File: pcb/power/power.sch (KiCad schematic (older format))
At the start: 48 parts, among them CON1 BARREL_JACK, P1 CONN_01X04, P2 CONN_01X04, P3 CONN_01X04, P4 USB_B, P5 CONN_01X03, P6 CONN_01X03, U1 TS30013, U2 LM324QT, U3 LM2840

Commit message: Added some more footprints. Maybe have to change some grounding stuff.
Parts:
- removed D4: VS-10MQ060NPbF, symbol D_Schottky
- removed P1: CONN_01X04, symbol CONN_01X04
- removed P4: USB_B, symbol USB_B
- removed P6: CONN_01X03, symbol CONN_01X03
- removed U1: TS30013, symbol TS30013
- added D?: VS-10MQ060NPbF, Diodes_SMD:SMA_Handsoldering, symbol D_Schottky
- added P?: USB_A, Connect:USB_A, symbol USB_A
- added P?: CONN_01X04, Pin_Headers:Pin_Header_Straight_1x04, symbol CONN_01X04
- added P?: CONN_01X03, Pin_Headers:Pin_Header_Straight_1x03, symbol CONN_01X03
- added U?: TS30012, Additional:QFN-16-1EP_3x3mm_Pitch0.5mm, symbol TS30012
- C1, C11, C2, C3, C4, C6, C8: footprint (none) -> Capacitors_SMD:C_0603_HandSoldering
- D2: footprint (none) -> Diodes_SMD:SMA_Handsoldering
- D3, D5: footprint (none) -> LEDs:LED_0603
- L1: footprint (none) -> Additional:Taiyo_Yuden_NRS8030_IND
- L2: footprint (none) -> Additional:Bourns_SRN3015
- P2: footprint (none) -> Pin_Headers:Pin_Header_Straight_1x04; Digikey (none) -> S7002-ND
- P5: footprint (none) -> Pin_Headers:Pin_Header_Straight_1x03; Digikey (none) -> S7036-ND
- R10, R11, R12: footprint (none) -> Resistors_SMD:R_0603_HandSoldering
- R20: Digikey (none) -> 311-560GRCT-ND
- R6: footprint (none) -> Capacitors_SMD:C_0603_HandSoldering; Digikey (none) -> 311-1.5KGRCT-ND
- U3: footprint (none) -> TO_SOT_Packages_SMD:SOT-23-6
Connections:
- net labels added: GNDPWR
- wire segments 142 -> 140
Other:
- note added: "5V for Mobile Phone\n-----------------------\nVout,max=5 V\nAout,max = 2A"
- note added: "Bucket Converter\n---------------------------\nVout=0.765 V (1 + (27k/ 10.15k))=2.8 V\n27k/10.15k= 2.66"
- note removed: "Bucket Converter\n---------------------------\nVout=0.765 V (1 + (27k/ 10.15k))=2.8 V\n27k/10.15= 2.66"
- moved on the sheet: R6

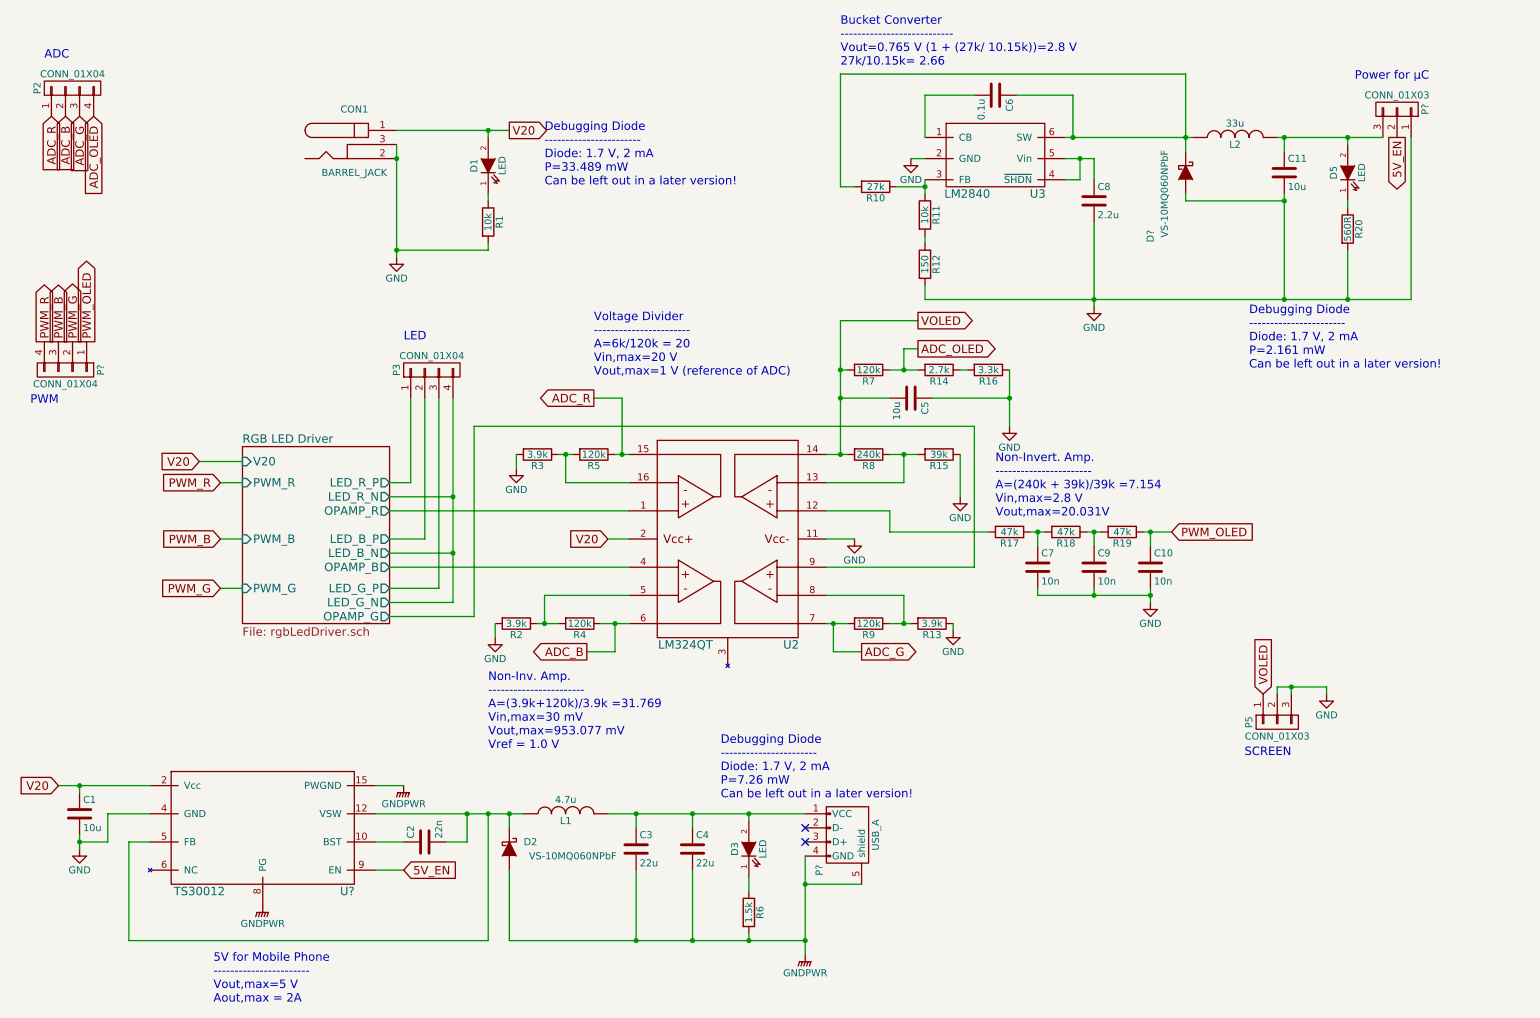
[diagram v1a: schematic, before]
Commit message: All footprints assigned. No DRC errors anymore.
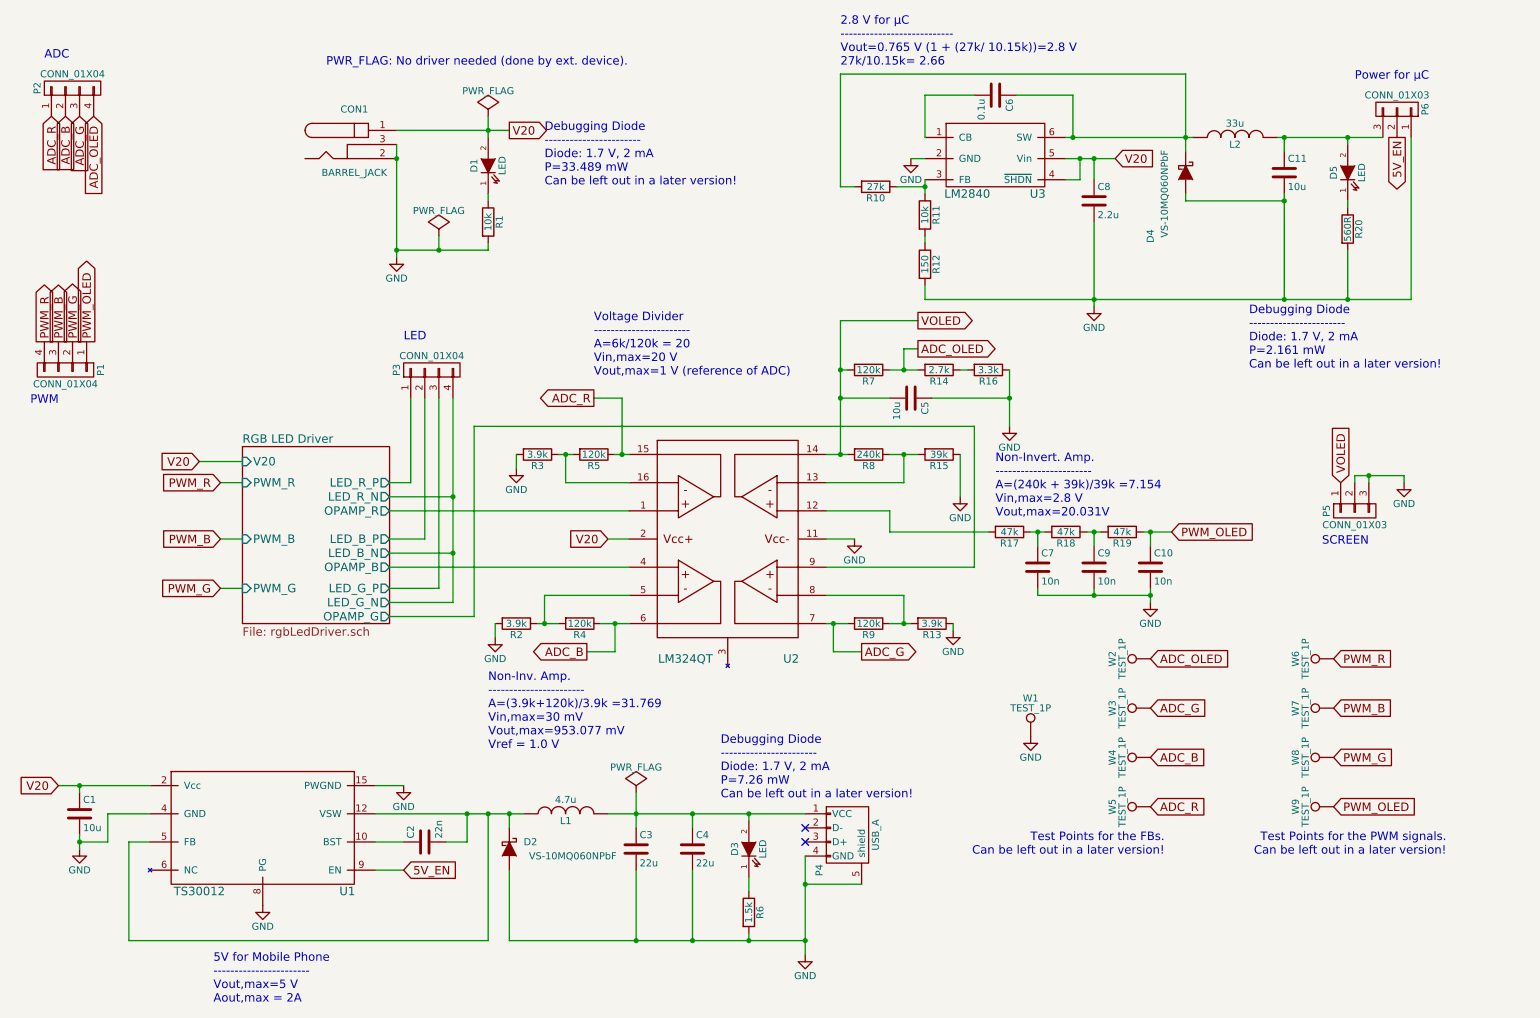
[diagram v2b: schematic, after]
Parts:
- added W1: TEST_1P, Measurement_Points:Measurement_Point_Round-SMD-Pad_Big, symbol TEST_1P
- added W2, W3, W4, W5, W6, W7, W8, W9: TEST_1P, Additional:TP_PROBE, symbol TEST_1P
- C10, C5, C7, C9: footprint (none) -> Capacitors_SMD:C_0603_HandSoldering
- D1: footprint (none) -> LEDs:LED_0603
- P3: footprint (none) -> Connect:PINHEAD1-3; Digikey ED2611-ND -> ED10563-ND
- R1: footprint (none) -> Resistors_SMD:R_0603_HandSoldering; Digikey (none) -> 311-10.0KHRCT-ND
- R13, R14, R15, R16, R17, R18, R19, R2, R20, R3, R4, R5, R7, R8, R9: footprint (none) -> Resistors_SMD:R_0603_HandSoldering
- U2: footprint (none) -> Additional:QFN-16-1EP_3x3mm_Pitch0.5mm
- gave numbers to parts that had none: 5
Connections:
- net GNDPWR is gone; now on net GND: C3.2, C4.2, D2.2 (A), P4.4 (GND), P4.5 (shield), R6.2, U1.14 (PWGND), U1.15 (PWGND), U1.8 (PG)
- net ADC_B: now also W4.1
- net ADC_G: now also W3.1
- net ADC_OLED: now also W2.1
- net ADC_R: now also W5.1
- net GND: now also W1.1
- net PWM_B: now also W7.1
- net PWM_G: now also W8.1
- net PWM_OLED: now also W9.1
- net PWM_R: now also W6.1
- net Vcc: now also C8.1, U3.4 (~SHDN), U3.5 (Vin)
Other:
- note added: "2.8 V for µC\n---------------------------\nVout=0.765 V (1 + (27k/ 10.15k))=2.8 V\n27k/10.15k= 2.66"
- note added: "PWR_FLAG: No driver needed (done by ext. device)."
- note added: "Test Points for the FBs.\nCan be left out in a later version!"
- note added: "Test Points for the PWM signals.\nCan be left out in a later version!"
- note removed: "Bucket Converter\n---------------------------\nVout=0.765 V (1 + (27k/ 10.15k))=2.8 V\n27k/10.15k= 2.66"
- moved on the sheet: P5

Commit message: Finished the schematics.
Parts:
- removed C1, C11, C5: 10u, Capacitors_SMD:C_0603_HandSoldering, symbol C
- removed C10, C7, C9: 10n, Capacitors_SMD:C_0603_HandSoldering, symbol C
- removed C2: 22n, Capacitors_SMD:C_0603_HandSoldering, symbol C
- removed C3, C4: 22u, Capacitors_SMD:C_0603_HandSoldering, symbol C
- removed C6: 0.1u, Capacitors_SMD:C_0603_HandSoldering, symbol C
- removed C8: 2.2u, Capacitors_SMD:C_0603_HandSoldering, symbol C
- removed D2, D4: VS-10MQ060NPbF, Diodes_SMD:SMA_Handsoldering, symbol D_Schottky
- removed D3, D5: LED, LEDs:LED_0603, symbol LED
- removed L1: 4.7u, Additional:Taiyo_Yuden_NRS8030_IND, symbol INDUCTOR
- removed L2: 33u, Additional:Bourns_SRN3015, symbol INDUCTOR
- removed P3: CONN_01X04, Connect:PINHEAD1-3, symbol CONN_01X04
- removed P6: CONN_01X03, Pin_Headers:Pin_Header_Straight_1x03, symbol CONN_01X03
- removed R10: 27k, Resistors_SMD:R_0603_HandSoldering, symbol R
- removed R11: 10k, Resistors_SMD:R_0603_HandSoldering, symbol R
- removed R12: 150, Resistors_SMD:R_0603_HandSoldering, symbol R
- removed R13, R2, R3: 3.9k, Resistors_SMD:R_0603_HandSoldering, symbol R
- removed R14: 2.7k, Resistors_SMD:R_0603_HandSoldering, symbol R
- removed R15: 39k, Resistors_SMD:R_0603_HandSoldering, symbol R
- removed R16: 3.3k, Resistors_SMD:R_0603_HandSoldering, symbol R
- removed R17, R18, R19: 47k, Resistors_SMD:R_0603_HandSoldering, symbol R
- removed R20: 560R, Resistors_SMD:R_0603_HandSoldering, symbol R
- removed R4, R5, R7, R9: 120k, Resistors_SMD:R_0603_HandSoldering, symbol R
- removed R6: 1.5k, Capacitors_SMD:C_0603_HandSoldering, symbol R
- removed R8: 240k, Resistors_SMD:R_0603_HandSoldering, symbol R
- removed U1: TS30012, Additional:QFN-16-1EP_3x3mm_Pitch0.5mm, symbol TS30012
- removed U2: LM324QT, Additional:QFN-16-1EP_3x3mm_Pitch0.5mm, symbol LM324QT
- removed U3: LM2840, TO_SOT_Packages_SMD:SOT-23-6, symbol LM2840
- removed W1: TEST_1P, Measurement_Points:Measurement_Point_Round-SMD-Pad_Big, symbol TEST_1P
- removed W2, W3, W4, W5, W6, W7, W8, W9: TEST_1P, Additional:TP_PROBE, symbol TEST_1P
- added P3: CONN_01X03, Pin_Headers:Pin_Header_Straight_1x03, symbol CONN_01X03
- renumbered P2 to P1, P1 to P2
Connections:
- net 5V_EN: now also P3.2 (P2)
- net GND: now also P3.1 (P1)
- net PWM_B: now also P2.2 (P2); no longer P2.3 (P3)
- net PWM_G: now also P2.3 (P3); no longer P2.2 (P2)
- net PWM_OLED: now also P2.4 (P4); no longer P2.1 (P1)
- net PWM_R: now also P2.1 (P1); no longer P2.4 (P4)
- net V5: now reaches P4.1 (VCC)
- net Vcc renamed V20
- new net V28: P3.3 (P3)
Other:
- note removed: "2.8 V for µC\n---------------------------\nVout=0.765 V (1 + (27k/ 10.15k))=2.8 V\n27k/10.15k= 2.66"
- note removed: "5V for Mobile Phone\n-----------------------\nVout,max=5 V\nAout,max = 2A"
- note removed: "Debugging Diode\n-----------------------\nDiode: 1.7 V, 2 mA\nP=2.161 mW\nCan be left out in a later version!"
- note removed: "Debugging Diode\n-----------------------\nDiode: 1.7 V, 2 mA\nP=7.26 mW\nCan be left out in a later version!"
- note removed: "LED"
- note removed: "Non-Inv. Amp.\n-----------------------\nA=(3.9k+120k)/3.9k =31.769\nVin,max=30 mV\nVout,max=953.077 mV\nVref = 1.0 V"
- note removed: "Non-Invert. Amp.\n-----------------------\nA=(240k + 39k)/39k =7.154\nVin,max=2.8 V\nVout,max=20.031V"
- note removed: "Test Points for the FBs.\nCan be left out in a later version!"
- note removed: "Test Points for the PWM signals.\nCan be left out in a later version!"
- note removed: "Voltage Divider\n-----------------------\nA=6k/120k = 20\nVin,max=20 V\nVout,max=1 V (reference of ADC)"
- moved on the sheet: CON1, D1, P1, P2, P5, R1

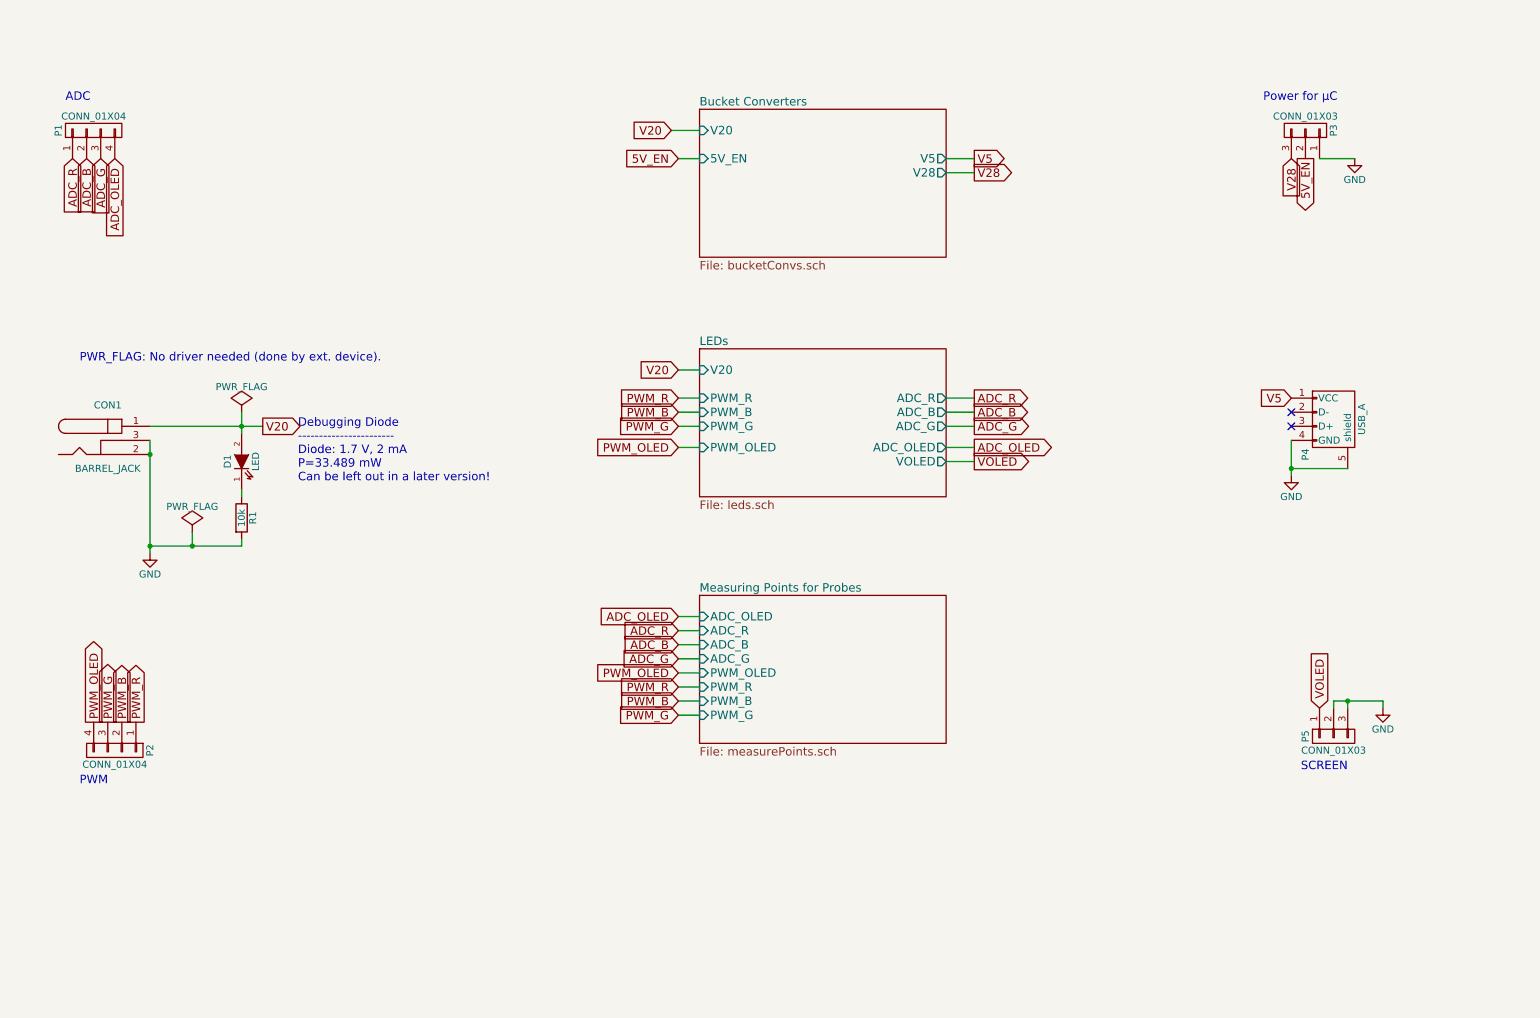
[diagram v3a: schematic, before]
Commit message: Started layouting. Interfacing problems have to be discussed.
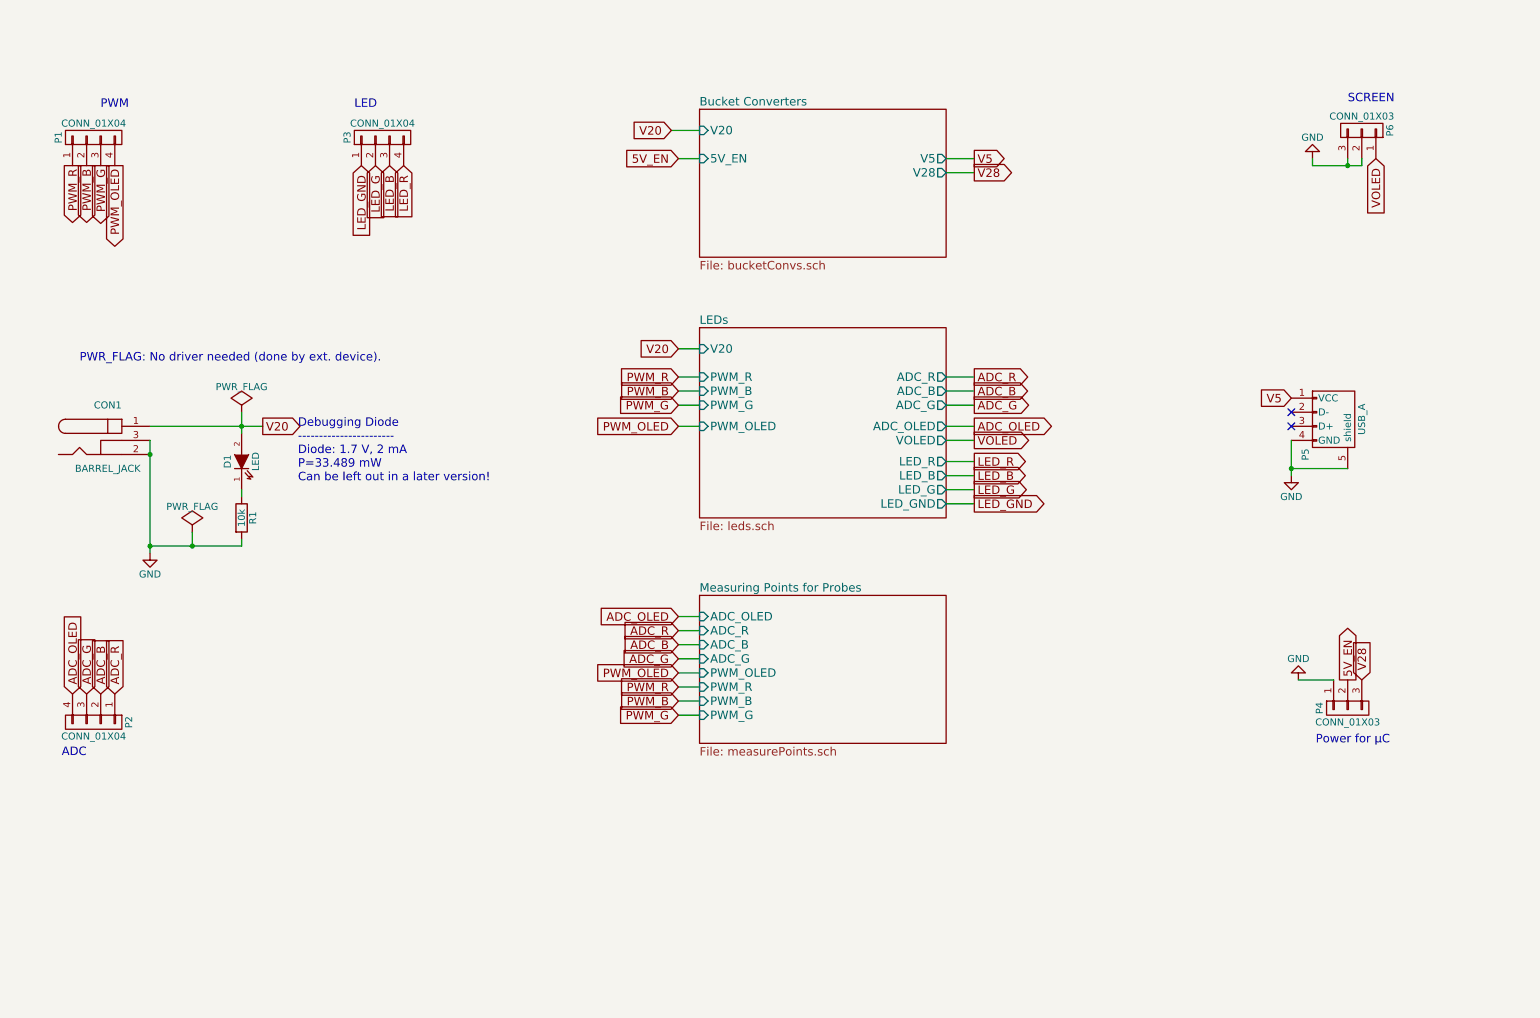
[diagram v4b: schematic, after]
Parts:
- added P3: CONN_01X04, Pin_Headers:Pin_Header_Straight_1x04, symbol CONN_01X04
- renumbered P2 to P1, P1 to P2, P3 to P4, P4 to P5, P5 to P6
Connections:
- new net LED_B: P3.3 (P3)
- new net LED_G: P3.2 (P2)
- new net LED_GND: P3.1 (P1)
- new net LED_R: P3.4 (P4)
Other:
- note added: "LED"
- moved on the sheet: P1, P2, P4, P6
